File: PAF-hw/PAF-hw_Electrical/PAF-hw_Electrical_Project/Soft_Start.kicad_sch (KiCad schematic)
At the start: 7 parts, among them Q1 NDT452AP

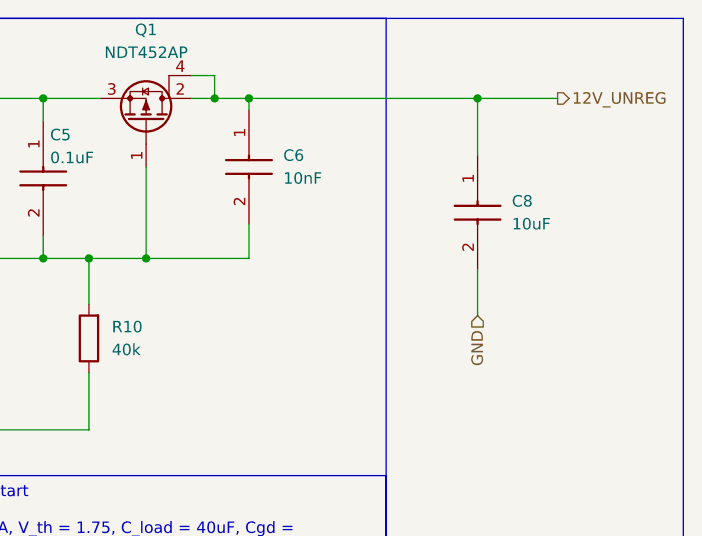
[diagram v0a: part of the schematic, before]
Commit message: Added motor driver to schematic.
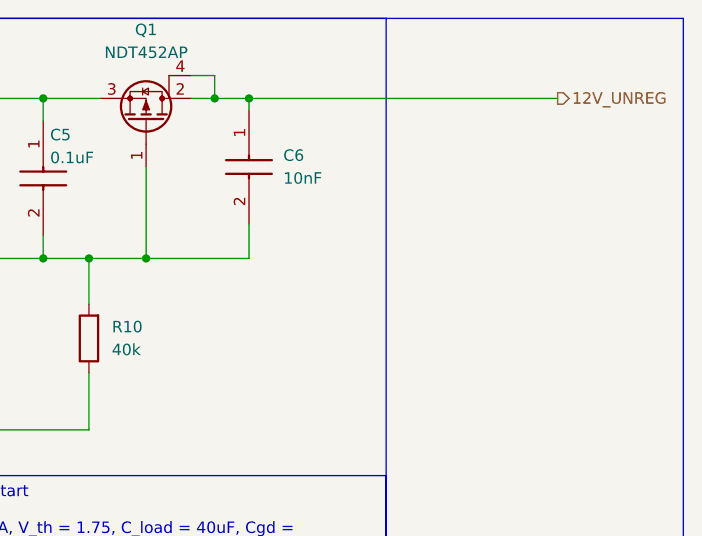
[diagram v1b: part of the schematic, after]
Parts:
- removed C8: 10uF, CAPC2012X145N, symbol SamacSys_Parts:CL21A106KAYNNNE
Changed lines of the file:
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@@
-	)
-	(junction
-		(at 193.04 66.04)
-		(diameter 0)
-		(color 0 0 0 0)
 	)
 	(junction
@@
 	(wire
 		(pts
-			(xy 193.04 85.09) (xy 193.04 90.17)
-		)
-		(stroke
-			(width 0)
-			(type default)
-		)
-	)
-	(wire
-		(pts
 			(xy 114.3 95.25) (xy 114.3 102.87)
 		)
@@
 	(wire
 		(pts
-			(xy 193.04 66.04) (xy 193.04 72.39)
-		)
-		(stroke
-			(width 0)
-			(type default)
-		)
-	)
-	(wire
-		(pts
 			(xy 163.83 63.5) (xy 163.83 66.04)
 		)
@@
 	(wire
 		(pts
-			(xy 167.64 66.04) (xy 193.04 66.04)
+			(xy 167.64 66.04) (xy 201.93 66.04)
 		)
 		(stroke
@@
 		(pts
 			(xy 156.21 83.82) (xy 167.64 83.82)
-		)
-		(stroke
-			(width 0)
-			(type default)
-		)
-	)
-	(wire
-		(pts
-			(xy 193.04 66.04) (xy 201.93 66.04)
 		)
 		(stroke
@@
 		(shape input)
 		(at 100.33 66.04 180)
-		(effects
-			(font
-				(size 1.27 1.27)
-			)
-			(justify right)
-		)
-	)
-	(hierarchical_label "GND"
-		(shape input)
-		(at 193.04 90.17 270)
 		(effects
 			(font
@@
 					(unit 1)
 				)
-			)
-		)
-	)
-	(symbol
-		(lib_id "SamacSys_Parts:CL21A106KAYNNNE")
-		(at 193.04 72.39 270)
-		(unit 1)
-		(exclude_from_sim no)
-		(in_bom yes)
-		(on_board yes)
-		(dnp no)
-		(property "Reference" "C8"
-			(at 196.85 77.4699 90)
-			(effects
-				(font
-					(size 1.27 1.27)
-				)
-				(justify left)
-			)
-		)
-		(property "Value" "10uF"
-			(at 196.85 80.0099 90)
-			(effects
-				(font
-					(size 1.27 1.27)
-				)
-				(justify left)
-			)
-		)
-		(property "Footprint" "CAPC2012X145N"
-			(at 204.978 71.12 0)
-			(effects
-				(font
-					(size 1.27 1.27)
-				)
-				(justify left top)
-				(hide yes)
-			)
-		)
-		(property "Datasheet" "https://datasheet.datasheetarchive.com/originals/distributors/Datasheets_SAMA/6a45835c9b7400e9b49c55c38a8ff4a2.pdf"
-			(at -3.15 81.28 0)
-			(effects
-				(font
-					(size 1.27 1.27)
-				)
-				(justify left top)
-				(hide yes)
-			)
-		)
-		(property "Description" "Samsung"
-			(at 193.04 72.39 0)
-			(effects
-				(font
-					(size 1.27 1.27)
-				)
-				(hide yes)
-			)
-		)
-		(property "Height" "1.45"
-			(at -203.15 81.28 0)
-			(effects
-				(font
-					(size 1.27 1.27)
-				)
-				(justify left top)
-				(hide yes)
-			)
-		)
-		(property "Manufacturer_Name" "SAMSUNG"
-			(at -303.15 81.28 0)
-			(effects
-				(font
-					(size 1.27 1.27)
-				)
-				(justify left top)
-				(hide yes)
-			)
-		)
-		(property "Manufacturer_Part_Number" "CL21A106KAYNNNE"
-			(at -403.15 81.28 0)
-			(effects
-				(font
-					(size 1.27 1.27)
-				)
-				(justify left top)
-				(hide yes)
-			)
-		)
-		(property "Mouser Part Number" "187-CL21A106KAYNNNE"
-			(at -503.15 81.28 0)
-			(effects
-				(font
-					(size 1.27 1.27)
-				)
-				(justify left top)
-				(hide yes)
-			)
-		)
-		(property "Mouser Price/Stock" "https://www.mouser.co.uk/ProductDetail/Samsung-Electro-Mechanics/CL21A106KAYNNNE?qs=yOVawPpwOwmTXAd4dJtNjA%3D%3D"
-			(at -603.15 81.28 0)
-			(effects
-				(font
-					(size 1.27 1.27)
-				)
-				(justify left top)
-				(hide yes)
-			)
-		)
-		(property "Arrow Part Number" "CL21A106KAYNNNE"
-			(at -703.15 81.28 0)
-			(effects
-				(font
-					(size 1.27 1.27)
-				)
-				(justify left top)
-				(hide yes)
-			)
-		)
-		(property "Arrow Price/Stock" "https://www.arrow.com/en/products/cl21a106kaynnne/samsung-electro-mechanics?utm_currency=USD&region=nac"
-			(at -803.15 81.28 0)
-			(effects
-				(font
-					(size 1.27 1.27)
-				)
-				(justify left top)
-				(hide yes)
-			)
-		)
-		(pin "1"
-		)
-		(pin "2"
-		)
-		(instances
-			(project "PAF-hw_Electrical_Project"
-				(path "/c6f2fd82-4900-4fc0-ba31-c37e114de4ed/5b2f8001-20dc-46f2-9b58-1fe2aab2ff9d"
-					(reference "C8")
-					(unit 1)
-				)

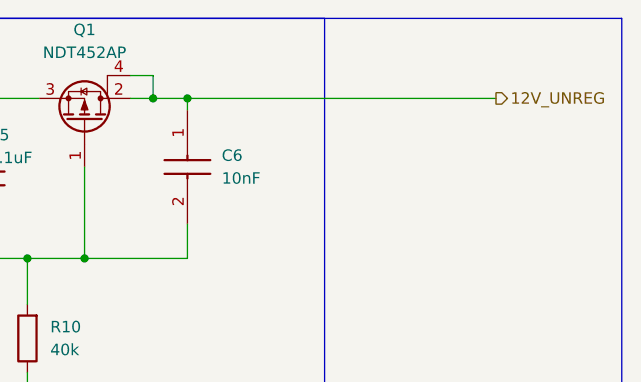
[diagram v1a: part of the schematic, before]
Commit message: Added camera circuit to schematic.
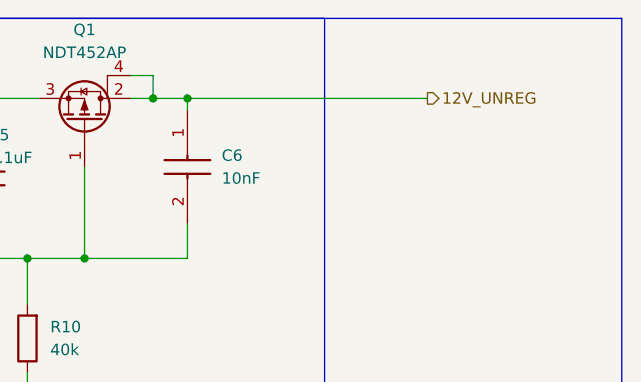
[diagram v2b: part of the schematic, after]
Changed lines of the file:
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@@
 	(wire
 		(pts
-			(xy 167.64 66.04) (xy 201.93 66.04)
+			(xy 167.64 66.04) (xy 194.31 66.04)
 		)
 		(stroke
@@
 	(hierarchical_label "12V_UNREG"
 		(shape output)
-		(at 201.93 66.04 0)
+		(at 194.31 66.04 0)
 		(effects
 			(font
